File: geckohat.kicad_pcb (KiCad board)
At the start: 2 copper layers, 65 x 56 mm, 36 parts, among them J1 CONN_02X20, J2 TEST_1P, U1 EFM32JG1B100F128GM32, U2 LP2985LV, Y1 38.4 MHz, Y2 32kHz

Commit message: Get rid of grounded copper around holes
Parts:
- added G***: LOGO, elemental:elemental-4mm-mask, F.Cu at (181.6, 80.4)
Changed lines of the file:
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@@
     (links 186)
     (no_connects 17)
-    (area 117.268571 69.995 187.000001 129.465)
+    (area 121.094999 71.354999 186.245001 127.505001)
     (thickness 1.6)
     (drawings 22)
     (tracks 700)
     (zones 0)
-    (modules 36)
+    (modules 37)
     (nets 92)
   )
@@
     (36 B.SilkS user)
     (37 F.SilkS user)
-    (38 B.Mask user)
+    (38 B.Mask user hide)
     (39 F.Mask user)
     (40 Dwgs.User user)
@@
     )
   )
-  (module holes:hole_2.75 locked (layer F.Cu)
-    (at 124.67 74.93)
-    (fp_text reference REF** (at 0 4.5) (layer F.SilkS) hide
-      (effects (font (size 1 1) (thickness 0.15)))
-    )
-    (fp_text value hole_2.75 (at 0 -4) (layer F.Fab) hide
-      (effects (font (size 1 1) (thickness 0.15)))
-    )
-    (fp_circle (center 0 0) (end 2.5 0) (layer F.Mask) (width 1.2))
-    (fp_circle (center 0 0) (end 2.5 0) (layer B.Mask) (width 1.2))
-    (pad "" np_thru_hole circle (at 0 0) (size 4 4) (drill 2.75) (layers *.Cu *.Mask))
-  )
-  (module holes:hole_2.75 locked (layer F.Cu)
-    (at 182.67 74.93)
-    (fp_text reference REF** (at 0 4.5) (layer F.SilkS) hide
-      (effects (font (size 1 1) (thickness 0.15)))
-    )
-    (fp_text value hole_2.75 (at 0 -4) (layer F.Fab) hide
-      (effects (font (size 1 1) (thickness 0.15)))
-    )
-    (fp_circle (center 0 0) (end 2.5 0) (layer F.Mask) (width 1.2))
-    (fp_circle (center 0 0) (end 2.5 0) (layer B.Mask) (width 1.2))
-    (pad "" np_thru_hole circle (at 0 0) (size 4 4) (drill 2.75) (layers *.Cu *.Mask))
-  )
-  (module holes:hole_2.75 locked (layer F.Cu)
-    (at 124.67 123.93)
-    (fp_text reference REF** (at 0 4.5) (layer F.SilkS) hide
-      (effects (font (size 1 1) (thickness 0.15)))
-    )
-    (fp_text value hole_2.75 (at 0 -4) (layer F.Fab) hide
-      (effects (font (size 1 1) (thickness 0.15)))
-    )
-    (fp_circle (center 0 0) (end 2.5 0) (layer F.Mask) (width 1.2))
-    (fp_circle (center 0 0) (end 2.5 0) (layer B.Mask) (width 1.2))
-    (pad "" np_thru_hole circle (at 0 0) (size 4 4) (drill 2.75) (layers *.Cu *.Mask))
-  )
-  (module holes:hole_2.75 locked (layer F.Cu)
-    (at 182.67 123.93)
-    (fp_text reference REF** (at 0 4.5) (layer F.SilkS) hide
-      (effects (font (size 1 1) (thickness 0.15)))
-    )
-    (fp_text value hole_2.75 (at 0 -4) (layer F.Fab) hide
-      (effects (font (size 1 1) (thickness 0.15)))
-    )
-    (fp_circle (center 0 0) (end 2.5 0) (layer F.Mask) (width 1.2))
-    (fp_circle (center 0 0) (end 2.5 0) (layer B.Mask) (width 1.2))
-    (pad "" np_thru_hole circle (at 0 0) (size 4 4) (drill 2.75) (layers *.Cu *.Mask))
-  )
   (module Wire_Pads:SolderWirePad_single_1mmDrill (layer F.Cu)
     (at 123 98)
@@
     (pad "" smd rect (at 0 0 270) (size 0.4 0.16) (layers F.Cu F.Paste F.Mask))
   )
+  (module elemental:elemental-4mm-mask (layer F.Cu)
+    (at 181.6 80.4)
+    (fp_text reference G*** (at 0 0) (layer F.SilkS) hide
+      (effects (font (thickness 0.3)))
+    )
+    (fp_text value LOGO (at 0.75 0) (layer F.SilkS) hide
+      (effects (font (thickness 0.3)))
+    )
+    (fp_poly (pts (xy 1.989666 1.989667) (xy 0.070555 1.989667) (xy -0.324633 1.989063) (xy -0.69361 1.987334)
+      (xy -1.027793 1.984605) (xy -1.318598 1.981) (xy -1.557443 1.976644) (xy -1.735743 1.97166)
+      (xy -1.844915 1.966173) (xy -1.876778 1.961445) (xy -1.882581 1.91458) (xy -1.887982 1.791632)
+      (xy -1.891581 1.651) (xy -1.609673 1.651) (xy 1.694339 1.651) (xy 1.683253 0.03175)
+      (xy 1.672166 -1.5875) (xy -1.5875 -1.5875) (xy -1.598587 0.03175) (xy -1.609673 1.651)
+      (xy -1.891581 1.651) (xy -1.892856 1.601185) (xy -1.89708 1.351823) (xy -1.900528 1.052127)
+      (xy -1.903077 0.710683) (xy -1.904601 0.336073) (xy -1.905 0.014111) (xy -1.905 -1.905)
+      (xy 1.989666 -1.905) (xy 1.989666 1.989667)) (layer F.Mask) (width 0.01))
+    (fp_poly (pts (xy -0.042334 -0.677333) (xy -0.973667 -0.677333) (xy -0.973667 -0.169333) (xy -0.254 -0.169333)
+      (xy -0.254 0.127) (xy -0.973667 0.127) (xy -0.973667 0.719667) (xy -0.042334 0.719667)
+      (xy -0.042334 1.016) (xy -1.27 1.016) (xy -1.27 -0.931333) (xy -0.042334 -0.931333)
+      (xy -0.042334 -0.677333)) (layer F.Mask) (width 0.01))
+    (fp_poly (pts (xy 0.592666 0.719667) (xy 1.439333 0.719667) (xy 1.439333 1.016) (xy 0.296333 1.016)
+      (xy 0.296333 -0.931333) (xy 0.592666 -0.931333) (xy 0.592666 0.719667)) (layer F.Mask) (width 0.01))
+  )
+  (module holes:hole_2.75 locked (layer F.Cu)
+    (at 124.67 74.93)
+    (fp_text reference REF** (at 0 4.5) (layer F.SilkS) hide
+      (effects (font (size 1 1) (thickness 0.15)))
+    )
+    (fp_text value hole_2.75 (at 0 -4) (layer F.Fab) hide
+      (effects (font (size 1 1) (thickness 0.15)))
+    )
+    (fp_circle (center 0 0) (end 2.5 0) (layer F.Mask) (width 1.2))
+    (fp_circle (center 0 0) (end 2.5 0) (layer B.Mask) (width 1.2))
+    (pad "" np_thru_hole circle (at 0 0) (size 6 6) (drill 2.75) (layers *.Cu *.Mask))
+  )
+  (module holes:hole_2.75 locked (layer F.Cu)
+    (at 182.67 74.93)
+    (fp_text reference REF** (at 0 4.5) (layer F.SilkS) hide
+      (effects (font (size 1 1) (thickness 0.15)))
+    )
+    (fp_text value hole_2.75 (at 0 -4) (layer F.Fab) hide
+      (effects (font (size 1 1) (thickness 0.15)))
+    )
+    (fp_circle (center 0 0) (end 2.5 0) (layer F.Mask) (width 1.2))
+    (fp_circle (center 0 0) (end 2.5 0) (layer B.Mask) (width 1.2))
+    (pad "" np_thru_hole circle (at 0 0) (size 6 6) (drill 2.75) (layers *.Cu *.Mask))
+  )
+  (module holes:hole_2.75 locked (layer F.Cu)
+    (at 124.67 123.93)
+    (fp_text reference REF** (at 0 4.5) (layer F.SilkS) hide
+      (effects (font (size 1 1) (thickness 0.15)))
+    )
+    (fp_text value hole_2.75 (at 0 -4) (layer F.Fab) hide
+      (effects (font (size 1 1) (thickness 0.15)))
+    )
+    (fp_circle (center 0 0) (end 2.5 0) (layer F.Mask) (width 1.2))
+    (fp_circle (center 0 0) (end 2.5 0) (layer B.Mask) (width 1.2))
+    (pad "" np_thru_hole circle (at 0 0) (size 6 6) (drill 2.75) (layers *.Cu *.Mask))
+  )
+  (module holes:hole_2.75 locked (layer F.Cu)
+    (at 182.67 123.93)
+    (fp_text reference REF** (at 0 4.5) (layer F.SilkS) hide
+      (effects (font (size 1 1) (thickness 0.15)))
+    )
+    (fp_text value hole_2.75 (at 0 -4) (layer F.Fab) hide
+      (effects (font (size 1 1) (thickness 0.15)))
+    )
+    (fp_circle (center 0 0) (end 2.5 0) (layer F.Mask) (width 1.2))
+    (fp_circle (center 0 0) (end 2.5 0) (layer B.Mask) (width 1.2))
+    (pad "" np_thru_hole circle (at 0 0) (size 6 6) (drill 2.75) (layers *.Cu *.Mask))
+  )
   (gr_text SCLK (at 129.5 88.5) (layer F.SilkS)

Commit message: Unknown changes that were lying around
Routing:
- net VDD: track 139.6 -> 134.2 mm

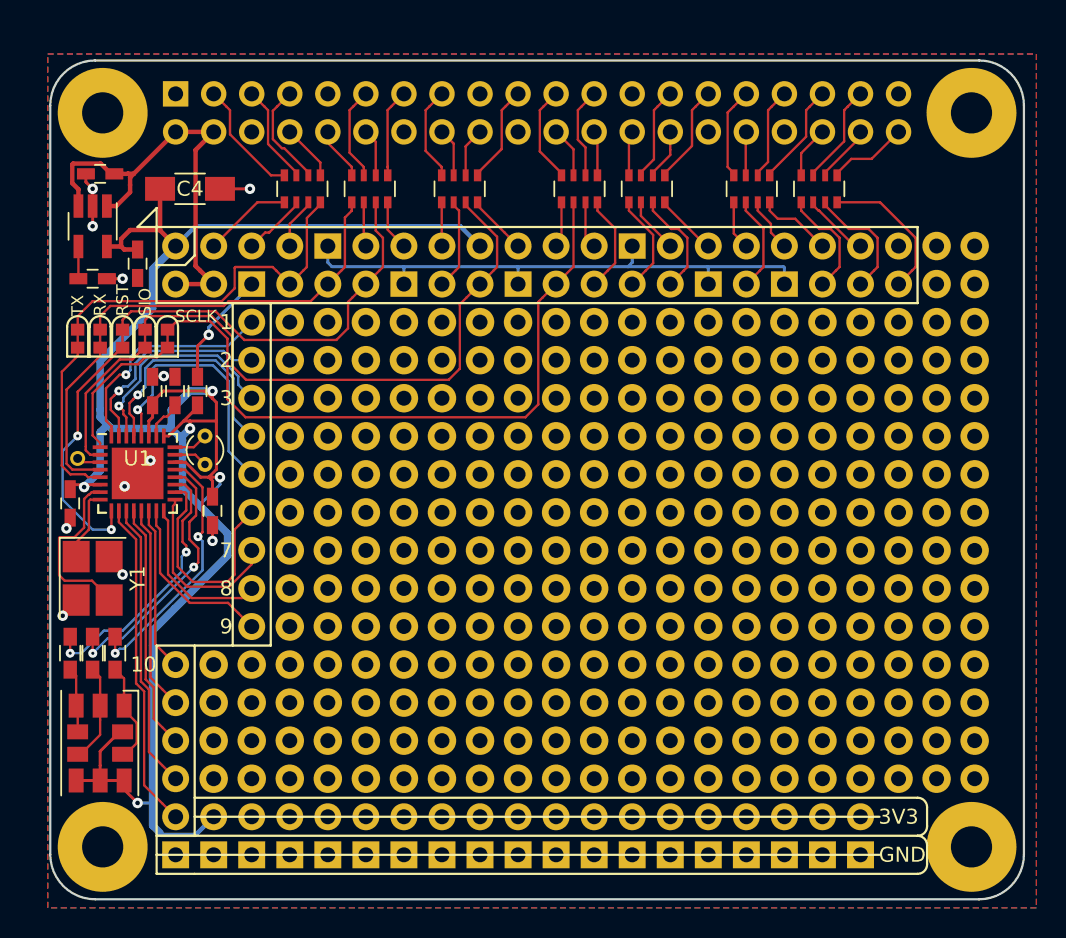
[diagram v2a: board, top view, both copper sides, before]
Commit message: Work on board: fix header rotation, LED, use discreet resistors
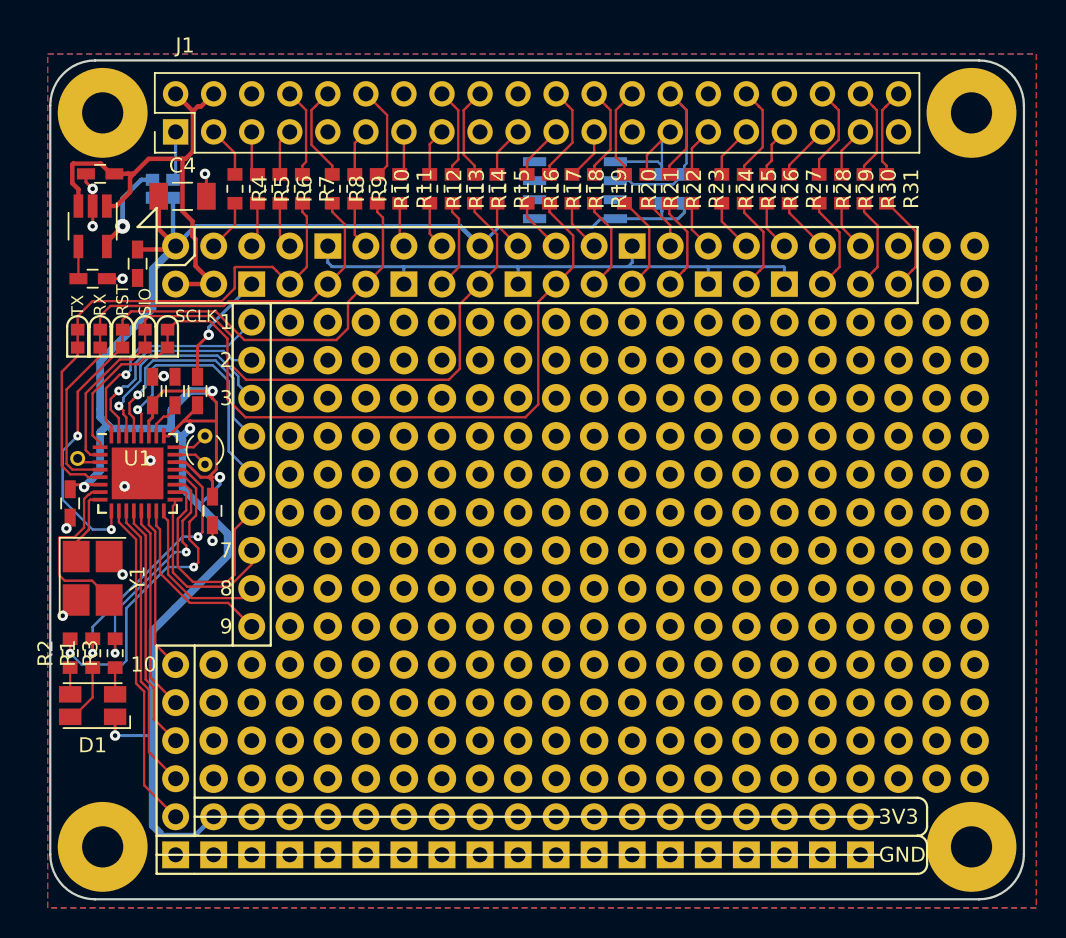
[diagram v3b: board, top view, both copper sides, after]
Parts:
- removed RN1, RN2, RN3, RN4, RN5, RN6, RN7: CAY16-221J4LF, Resistors_SMD:R_Array_Convex_4x0603
- added JP6: tie, tie:tie_0603, B.Cu at (128.0, 80.0)
- added JP7: Jumper_NO_Small, tie:tie_0603_open, B.Cu at (129.4, 80.0)
- added R10: R, r_local:R_0603_1608Metric_Pad0.84x1.00mm_HandSolder, F.Cu at (143.0, 80.0)
- added R11: R, r_local:R_0603_1608Metric_Pad0.84x1.00mm_HandSolder, F.Cu at (144.5, 80.0)
- added R12: R, r_local:R_0603_1608Metric_Pad0.84x1.00mm_HandSolder, F.Cu at (146.5, 80.0)
- added R13: R, r_local:R_0603_1608Metric_Pad0.84x1.00mm_HandSolder, F.Cu at (148.0, 80.0)
- added R14: R, r_local:R_0603_1608Metric_Pad0.84x1.00mm_HandSolder, F.Cu at (149.5, 80.0)
- added R15: R, r_local:R_0603_1608Metric_Pad0.84x1.00mm_HandSolder, F.Cu at (151.0, 80.0)
- added R16: R, r_local:R_0603_1608Metric_Pad0.84x1.00mm_HandSolder, F.Cu at (153.0, 80.0)
- added R17: R, r_local:R_0603_1608Metric_Pad0.84x1.00mm_HandSolder, F.Cu at (154.5, 80.0)
- added R18: R, r_local:R_0603_1608Metric_Pad0.84x1.00mm_HandSolder, F.Cu at (156.0, 80.0)
- added R19: R, r_local:R_0603_1608Metric_Pad0.84x1.00mm_HandSolder, F.Cu at (157.5, 80.0)
- added R20: R, r_local:R_0603_1608Metric_Pad0.84x1.00mm_HandSolder, F.Cu at (159.5, 80.0)
- added R21: R, r_local:R_0603_1608Metric_Pad0.84x1.00mm_HandSolder, F.Cu at (161.0, 80.0)
- added R22: R, r_local:R_0603_1608Metric_Pad0.84x1.00mm_HandSolder, F.Cu at (162.5, 80.0)
- added R23: R, r_local:R_0603_1608Metric_Pad0.84x1.00mm_HandSolder, F.Cu at (164.0, 80.0)
- added R24: R, r_local:R_0603_1608Metric_Pad0.84x1.00mm_HandSolder, F.Cu at (166.0, 80.0)
- added R25: R, r_local:R_0603_1608Metric_Pad0.84x1.00mm_HandSolder, F.Cu at (167.5, 80.0)
- added R26: R, r_local:R_0603_1608Metric_Pad0.84x1.00mm_HandSolder, F.Cu at (169.0, 80.0)
- added R27: R, r_local:R_0603_1608Metric_Pad0.84x1.00mm_HandSolder, F.Cu at (170.5, 80.0)
- added R28: R, r_local:R_0603_1608Metric_Pad0.84x1.00mm_HandSolder, F.Cu at (172.5, 80.0)
- added R29: R, r_local:R_0603_1608Metric_Pad0.84x1.00mm_HandSolder, F.Cu at (174.0, 80.0)
- added R30: R, r_local:R_0603_1608Metric_Pad0.84x1.00mm_HandSolder, F.Cu at (175.5, 80.0)
- added R31: R, r_local:R_0603_1608Metric_Pad0.84x1.00mm_HandSolder, F.Cu at (177.0, 80.0)
- added R32: 3k9, r_local:R_0603_1608Metric_Pad0.84x1.00mm_HandSolder, B.Cu at (163.5, 80.0)
- added R33: 3k9, r_local:R_0603_1608Metric_Pad0.84x1.00mm_HandSolder, B.Cu at (162.0, 80.0)
- added R4: R, r_local:R_0603_1608Metric_Pad0.84x1.00mm_HandSolder, F.Cu at (133.5, 80.0)
- added R5: R, r_local:R_0603_1608Metric_Pad0.84x1.00mm_HandSolder, F.Cu at (135.0, 80.0)
- added R6: R, r_local:R_0603_1608Metric_Pad0.84x1.00mm_HandSolder, F.Cu at (136.5, 80.0)
- added R7: R, r_local:R_0603_1608Metric_Pad0.84x1.00mm_HandSolder, F.Cu at (138.0, 80.0)
- added R8: R, r_local:R_0603_1608Metric_Pad0.84x1.00mm_HandSolder, F.Cu at (140.0, 80.0)
- added R9: R, r_local:R_0603_1608Metric_Pad0.84x1.00mm_HandSolder, F.Cu at (141.5, 80.0)
- added U3: CAT24C32, Housings_SOIC:SOIC-8_3.9x4.9mm_Pitch1.27mm, B.Cu at (156.2, 80.1)
- C4: footprint Capacitors_SMD:C_1206_HandSoldering -> c_local:C_1206_3216Metric_Pad1.24x1.80mm_HandSolder
- D1: value LED_RGB -> LED_ARGB; footprint led:LED_RGB_5050+PLCC4 -> led:LED_Avago_PLCC4_3.2x2.8mm_CW
- J1: moved to F.Cu
- R1, R2, R3: footprint Resistors_SMD:R_0603_HandSoldering -> r_local:R_0603_1608Metric_Pad0.84x1.00mm_HandSolder
- moved R3 3.00 mm to (125.5, 111.0)
- moved D1 2.55 mm to (124.0, 114.5), turned to 180 degrees
- moved J1 2.54 mm to (129.5, 76.2), turned to 90 degrees
- moved R1 1.50 mm to (124.0, 111.0)
- moved R2 1.50 mm to (122.5, 111.0)
- moved C4 0.71 mm to (130.0, 80.5)
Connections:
- D1 pad 1: Net-(D1-Pad1) -> VDD
- D1 pad 4: VDD -> Net-(D1-Pad4)
- J1 pad 1: (no net) -> /3V3_IN
- R1 pad 1: Net-(D1-Pad1) -> Net-(D1-Pad2)
- R1 pad 2: /LED_R -> /LED_B
- R2 pad 1: Net-(D1-Pad2) -> Net-(D1-Pad3)
- R3 pad 1: Net-(D1-Pad3) -> Net-(D1-Pad4)
- R3 pad 2: /LED_B -> /LED_R
- U1 pad 19: /LED_B -> /LED_R
- U1 pad 21: /LED_R -> /LED_B
- U2 pad 5: VDD -> /3V3_REG
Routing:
- net /ID_SC: track 3.38 -> 17.2 mm
- net VDD: track 134.2 -> 145.4 mm
- net Net-(D1-Pad1): track 6.75 -> 0.00 mm
- net /3V3_REG: track 0.00 -> 6.15 mm, vias 0 -> 1
- net /GPIO2: track 7.92 -> 3.43 mm
- net /ID_SD: track 6.25 -> 10.3 mm
- net /LED_G: track 18.3 -> 22.3 mm
- net /GPIO4: track 6.98 -> 3.11 mm
- net /GPIO3: track 6.67 -> 2.99 mm
- net /GPIO12: track 2.92 -> 6.34 mm
- net /GPIO26: track 6.75 -> 3.36 mm
- net /GPIO5: track 6.64 -> 3.29 mm
- net /GPIO8: track 2.99 -> 6.27 mm
- net /3V3_IN: track 0.00 -> 3.27 mm
- net /GPIO22: track 6.33 -> 3.18 mm
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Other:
- board text added: "2018"
- board text added: "Gecko RPi hat"

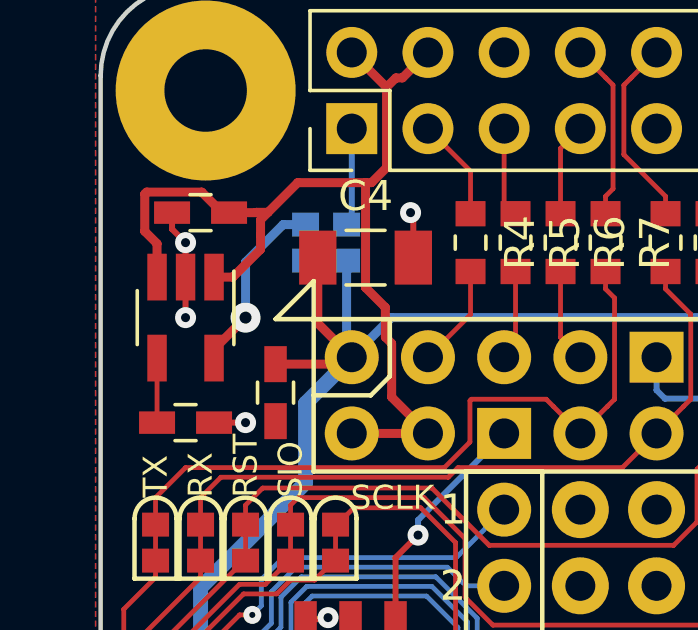
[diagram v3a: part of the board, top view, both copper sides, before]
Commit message: Replace a couple of cap footprints
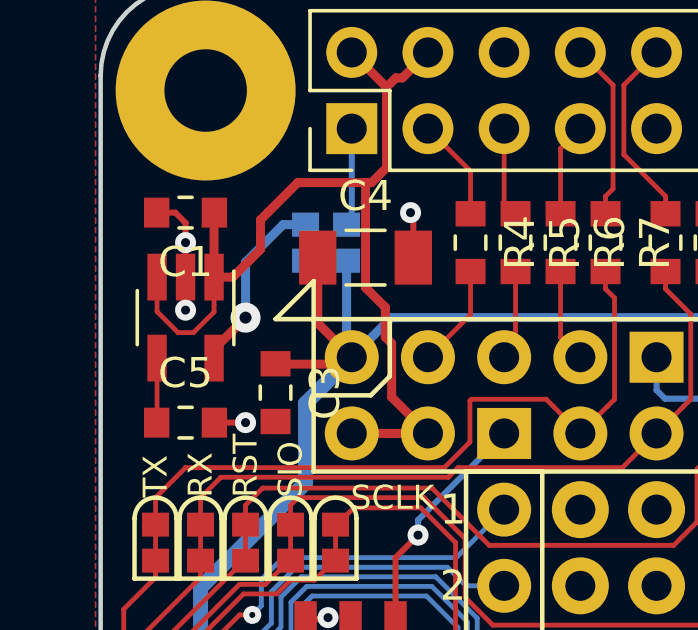
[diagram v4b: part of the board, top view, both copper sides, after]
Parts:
- C1, C3, C5: footprint Capacitors_SMD:C_0603_HandSoldering -> c_local:C_0603_1608Metric_Pad0.84x1.00mm_HandSolder
- moved C1 0.50 mm to (124.0, 79.0)
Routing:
- net GND: track 57.6 -> 58.2 mm

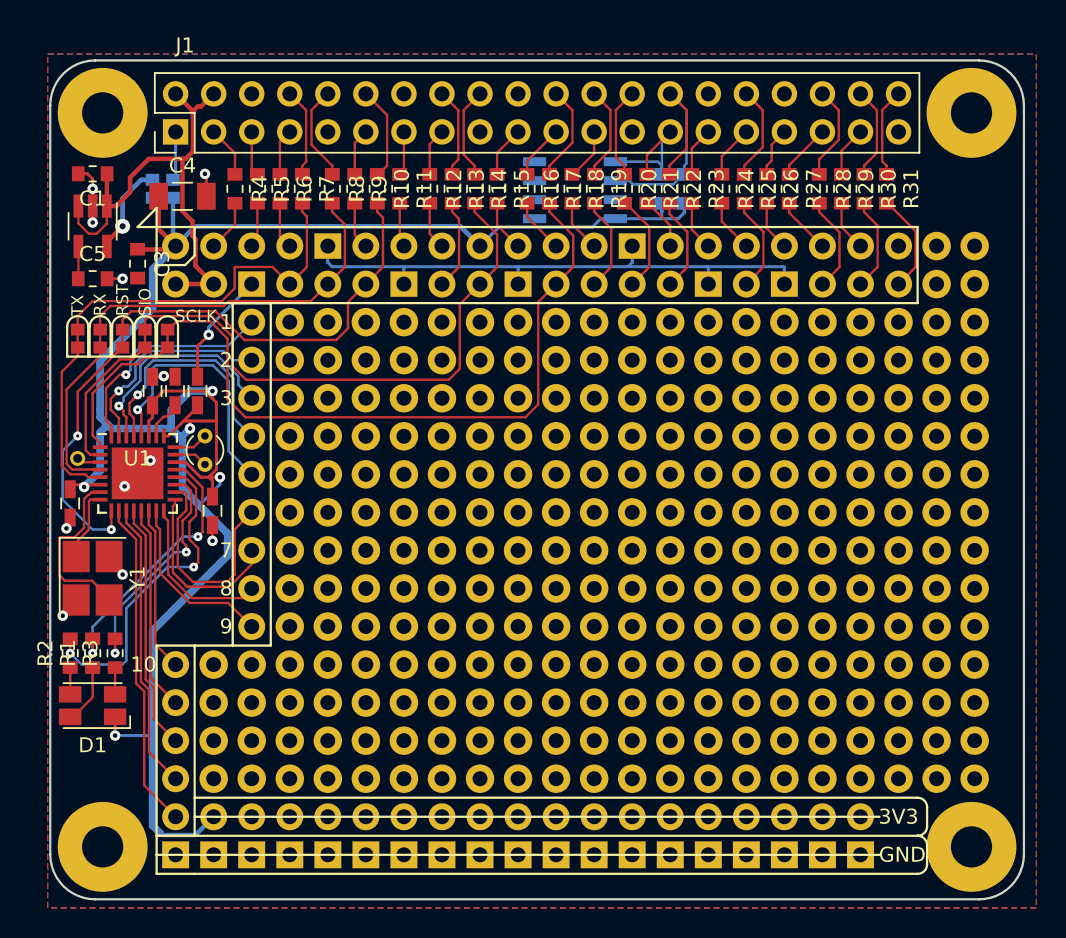
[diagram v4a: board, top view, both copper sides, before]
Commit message: Fix silkscreen
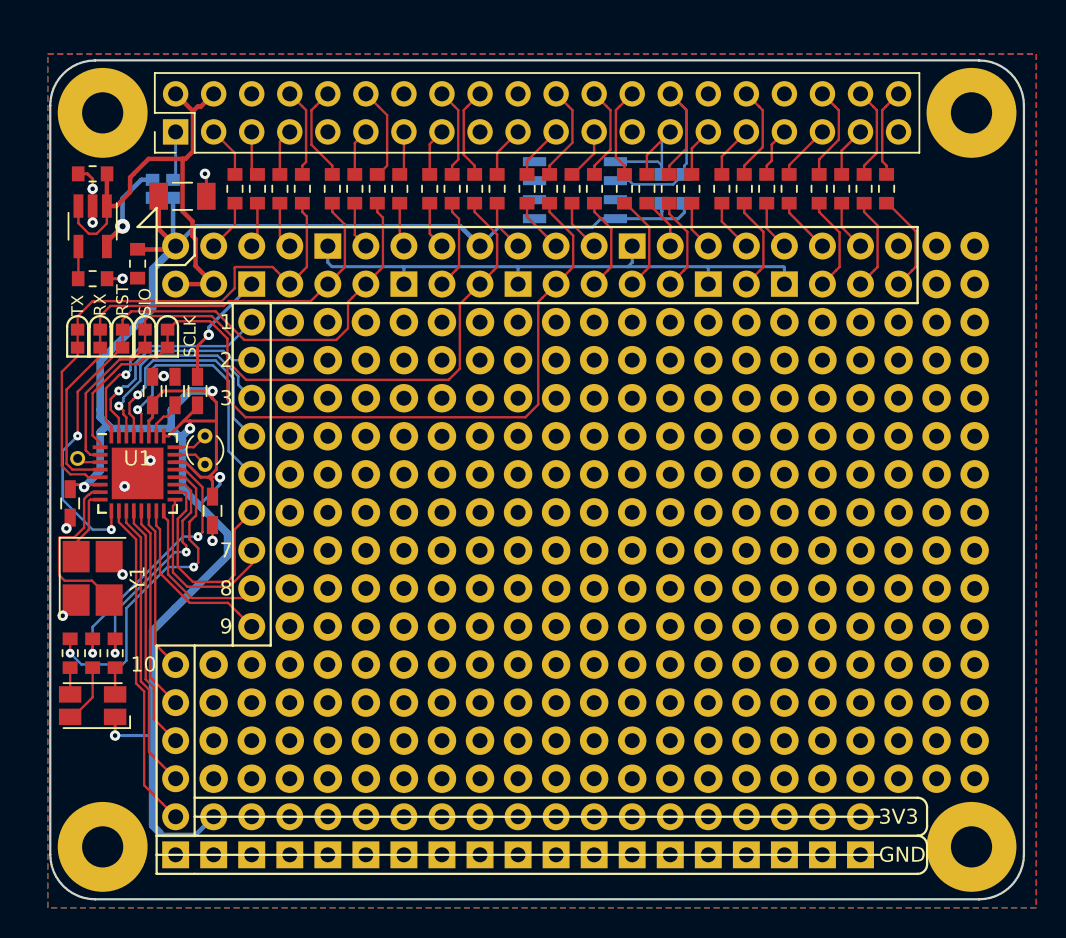
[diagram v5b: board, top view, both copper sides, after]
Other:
- board text added: "3.3V"
